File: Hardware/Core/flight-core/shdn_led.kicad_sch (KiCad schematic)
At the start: 4 parts, among them Q4 MMBF170

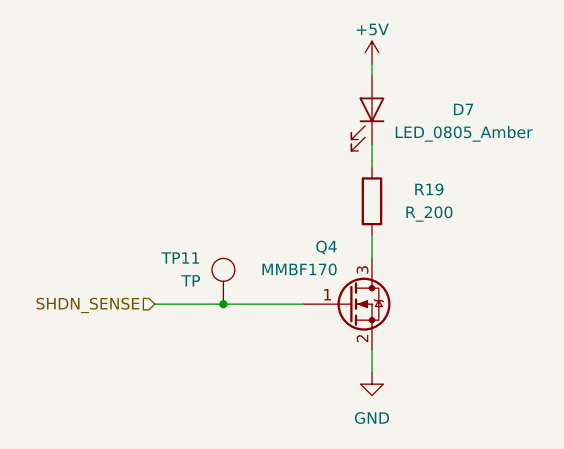
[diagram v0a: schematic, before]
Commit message: switching test points to correct footprint and alternative symbol, moving leds
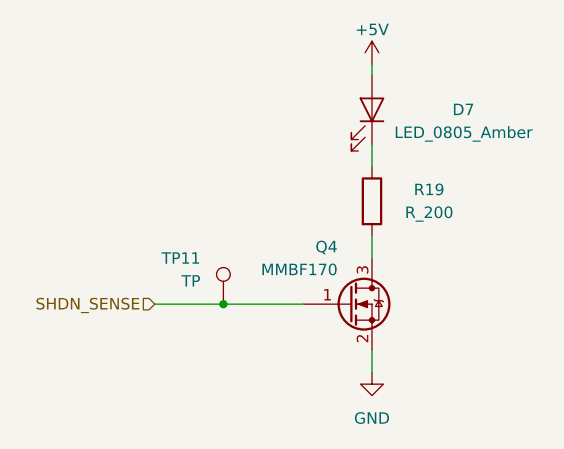
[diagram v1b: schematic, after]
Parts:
- TP11: footprint footprints:tp_1.6mm -> TestPoint:TestPoint_Pad_D1.0mm; symbol formula:TP -> OlinBAD:D1.0_TP
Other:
- moved on the sheet: TP11
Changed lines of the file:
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@@
 	)
 	(symbol
-		(lib_id "formula:TP")
-		(at 125.73 114.3 0)
+		(lib_id "OlinBAD:D1.0_TP")
+		(at 125.73 119.38 0)
 		(unit 1)
 		(exclude_from_sim no)
@@
 			)
 		)
-		(property "Footprint" "footprints:tp_1.6mm"
-			(at 123.19 116.84 0)
+		(property "Footprint" "TestPoint:TestPoint_Pad_D1.0mm"
+			(at 130.81 119.38 0)
 			(effects
 				(font
@@
 			)
 		)
-		(property "Datasheet" "http://www.keyelco.com/product-pdf.cfm?p=1314"
-			(at 125.73 114.3 0)
+		(property "Datasheet" "~"
+			(at 130.81 119.38 0)
 			(effects
 				(font
@@
 			)
 		)
-		(property "Description" ""
-			(at 125.73 114.3 0)
+		(property "Description" "test point"
+			(at 125.73 119.38 0)
 			(effects
 				(font
@@
 		)
 		(property "MFN" "DK"
-			(at 128.27 111.76 0)
+			(at 128.27 116.84 0)
 			(effects
 				(font
@@
 		)
 		(property "MPN" "36-5006-ND"
-			(at 130.81 109.22 0)
+			(at 130.81 114.3 0)
 			(effects
 				(font
@@
 		)
 		(property "PurchasingLink" "https://www.digikey.com/product-detail/en/keystone-electronics/5006/36-5006-ND/255330"
-			(at 133.35 106.68 0)
+			(at 133.35 111.76 0)
 			(effects
 				(font

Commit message: updating mini tps to new symbol and footprint
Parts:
- TP11: footprint TestPoint:TestPoint_Pad_D1.0mm -> obad_footprints:TestPoint_Pad_D1.0mm
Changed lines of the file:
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@@
 			)
 		)
-		(property "Footprint" "TestPoint:TestPoint_Pad_D1.0mm"
+		(property "Footprint" "obad_footprints:TestPoint_Pad_D1.0mm"
 			(at 130.81 119.38 0)
 			(effects

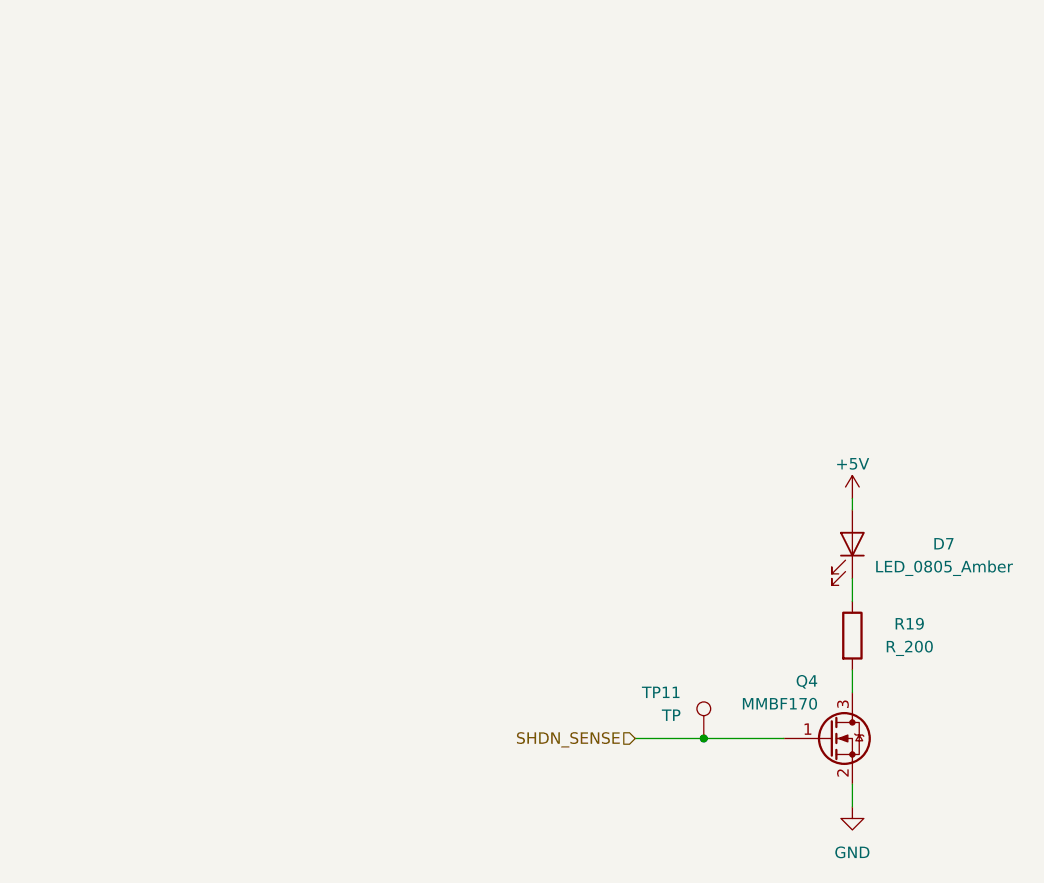
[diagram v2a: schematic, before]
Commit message: removed extra test points, removed debug2, reannotated schem
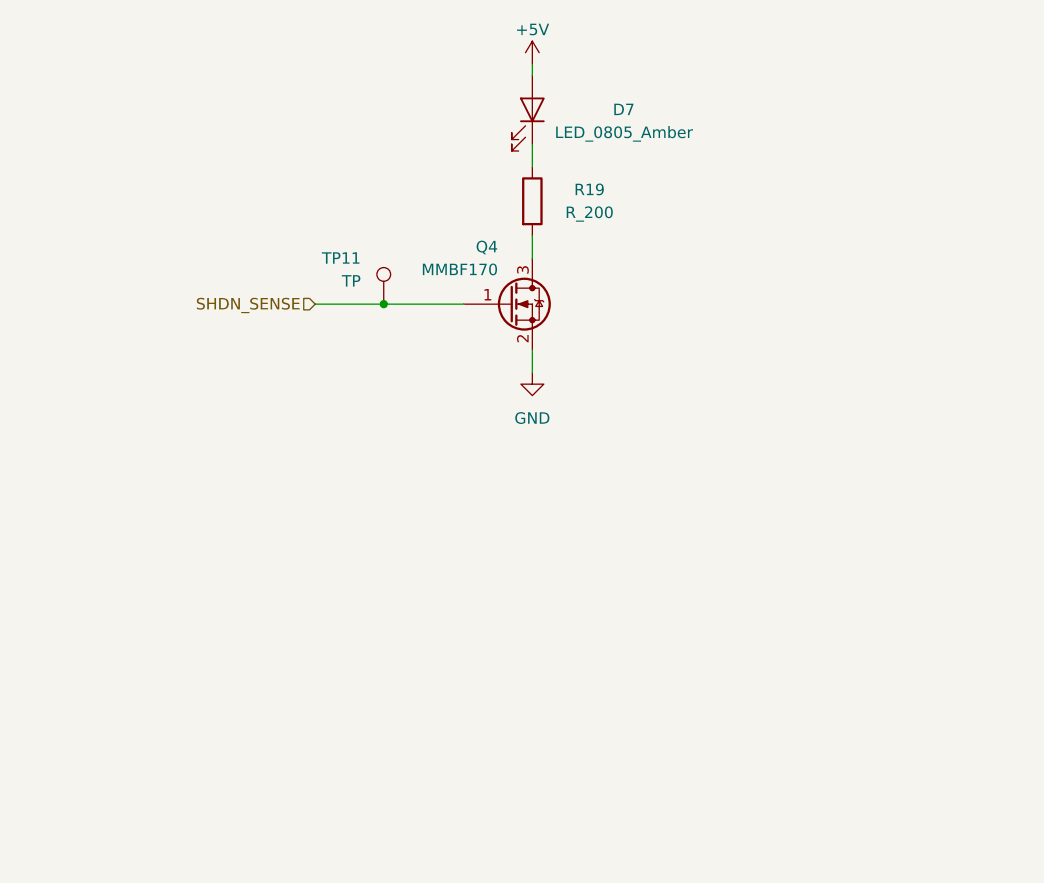
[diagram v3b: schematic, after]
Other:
- moved on the sheet: D7, Q4, R19, TP11

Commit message: Major reroute & semi-final update
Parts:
- removed TP11: TP, obad_footprints:TestPoint_Pad_D1.0mm, symbol OlinBAD:D1.0_TP
- added TP601: TP_ARMS_SHDN, TestPoint:TestPoint_Keystone_5019_Miniature, symbol formula:TP_SMD
- D7: value LED_0805_Amber -> LED_0805_BLUE
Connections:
- net SHDN_SENSE: now also TP601.1

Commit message: minor reformatting; no substantial changes
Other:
- note added: "Forgot a 100k pull-down attached to the SHDNs! Will be soldering these on by hand..."
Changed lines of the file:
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@@
 	(generator_version "9.0")
 	(paper "A5")
+	(text "Forgot a 100k pull-down attached to the SHDNs! \nWill be soldering these on by hand..."
+		(exclude_from_sim no)
+		(at 78.105 76.835 0)
+		(effects
+			(font
+				(size 1.27 1.27)
+			)
+		)
+	)
 	(junction
 		(at 88.9 71.12)
